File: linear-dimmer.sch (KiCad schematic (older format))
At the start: 32 parts, among them CON1 AVR-ISP-6, IC1 ATTINY85-S, P1 POWER, P2 OUTPUT, Q1 Q_NMOS_GDS, SW1 ENCODER, U1 LM78L05ACZ, U2 MCP6401

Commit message: Set some resistor values and FarnellIDs
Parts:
- R1: value R -> 10k
- R5: value R -> 220
- SW1: FarnellID (none) -> 2065047
- U2: FarnellID (none) -> 1852101
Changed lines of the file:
@@
 P 4950 4550
 F 0 "R1" V 5030 4550 50  0000 C CNN
-F 1 "R" V 4950 4550 50  0000 C CNN
+F 1 "10k" V 4950 4550 50  0000 C CNN
 F 2 "Resistors_SMD:R_0603_HandSoldering" V 4880 4550 30  0001 C CNN
 F 3 "" H 4950 4550 30  0000 C CNN
@@
 P 8600 3850
 F 0 "R5" V 8680 3850 50  0000 C CNN
-F 1 "R" V 8600 3850 50  0000 C CNN
+F 1 "220" V 8600 3850 50  0000 C CNN
 F 2 "Resistors_SMD:R_0603_HandSoldering" V 8530 3850 30  0001 C CNN
 F 3 "" H 8600 3850 30  0000 C CNN
@@
 F 2 "Housings_SOT-23_SOT-143_TSOT-6:SOT-23-5" H 7950 3850 60  0001 C CNN
 F 3 "" H 7950 3850 60  0000 C CNN
+F 4 "1852101" H 7950 3850 60  0001 C CNN "FarnellID"
 	1    7950 3850
 	1    0    0    -1
@@
 F 2 "" H 5850 5500 60  0000 C CNN
 F 3 "" H 5850 5500 60  0000 C CNN
+F 4 "2065047" H 5850 5500 60  0001 C CNN "FarnellID"
 	1    5850 5500
 	1    0    0    -1

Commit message: Redraw schematics with just a pot and an opamp current source
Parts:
- removed C5, C8: 1u, Capacitors_SMD:C_0603_HandSoldering, symbol C
- removed C6, C7: 2.2u, Capacitors_SMD:C_0603_HandSoldering, symbol C
- removed CON1: AVR-ISP-6, Pin_Headers:Pin_Header_Straight_2x03, symbol AVR-ISP-6
- removed IC1: ATTINY85-S, Housings_SOIC:SOIJ-8_5.3x5.3mm_Pitch1.27mm, symbol ATTINY85-S
- removed R10, R2, R8, R9: 10k, Resistors_SMD:R_0603_HandSoldering, symbol R
- removed R11, R13: 47k, Resistors_SMD:R_0603_HandSoldering, symbol R
- removed R12: 2.7k, Resistors_SMD:R_0603_HandSoldering, symbol R
- removed R3, R4: 220, Resistors_SMD:R_0603_HandSoldering, symbol R
- removed SW1: ENCODER, symbol ENCODER
- added R?: 36k, Resistors_SMD:R_0603_HandSoldering, symbol R
- added R?: 10k, Resistors_SMD:R_0603_HandSoldering, symbol R
- added RV1: 10k, symbol POT
- added U3: REF3012, Housings_SOT-23_SOT-143_TSOT-6:SOT-23_Handsoldering, symbol REF3012
- R1: value 10k -> 2k
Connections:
- net labels added: +1.2V
- wire segments 44 -> 19
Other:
- moved on the sheet: C1

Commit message: Add buffer opamp, choose a different opamp, redraw the PCB with dumb linead current source
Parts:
- removed U2: MCP6401, Housings_SOT-23_SOT-143_TSOT-6:SOT-23-5, symbol MCP6401
- added U2: MCP6072, Housings_SOIC:SOIC-8_3.9x4.9mm_Pitch1.27mm, symbol LM358N
- RV1: footprint (none) -> w_pth_resistors:trimmer_alps-rk09k1130ah1; FarnellID 191741 -> 1191725
- gave numbers to parts that had none: 2
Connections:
- wire segments 19 -> 23
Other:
- moved on the sheet: C1, C2, C3, C4, C9, D1, P1, P2, Q1, R1, R14, R2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

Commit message: Ready to send to PCB house
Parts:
- removed P2: OUTPUT, w_pin_strip:pin_socket_2, symbol CONN_01X02
- added C5, C6: 1u, Capacitors_SMD:C_0603_HandSoldering, symbol C
- added CON1: BARREL_JACK, symbol BARREL_JACK
- added D2: RED, w_smd_leds:Led_0603, symbol Led_Small
- added R10, R9: 10k, Resistors_SMD:R_0603_HandSoldering, symbol R
- added R11: 1M, Resistors_SMD:R_0603_HandSoldering, symbol R
- added R12: 220, Resistors_SMD:R_0603_HandSoldering, symbol R
- added R4: 3.74k, Resistors_SMD:R_0603_HandSoldering, symbol R
- added R8: 78.7k, Resistors_SMD:R_0603_HandSoldering, symbol R
- added SW1: Switch_SPDT_x2, Buttons_Switches_SMD:SW_SPDT_PCM12, symbol Switch_SPDT_x2
- added U4: MCP65R41T, w_smd_trans:sot23-6, symbol MCP65R41T-2402
- D1: value Led_Small -> BLUE
- Q1: value Q_NMOS_GDS -> BUK6207-55C; footprint w_smd_trans:sot223 -> w_smd_trans:d-pak; FarnellID 1769679 -> 1863263
- R2: value 36k -> 17.4k
- R6, R7: footprint Resistors_SMD:R_1206_HandSoldering -> Resistors_SMD:R_2512_HandSoldering; FarnellID 1576602 -> 1100070
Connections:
- net +1.2V: now also R10.1
- net +5V: now also C6.1, U4.6 (V+)
- net GND: now also C5.2, C6.2, D2.2 (C), R9.2, U4.2 (V-)
- net OUTPUT: now also C5.1, CON1.1
- net VCC: now also CON1.2, R8.1
- net at U2.6 (-), U2.7: now also SW1.2 (B); no longer R2.1
- net at R3.1, U2.3 (+): now also R2.1, R4.1; no longer R2.2
- new net: R2.2, SW1.3 (C)
- new net: R4.2, SW1.1 (A)
- new net: R11.2, R12.1, U4.1
- new net: D2.1 (A), R12.2
- new net: R8.2, R9.1, U4.3 (+)
- new net: R10.2, R11.1, U4.4 (_)
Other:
- note added: "1.25V"
- note added: "5mV hysteresis"
- note added: "Battery low detector. The lowest we go is 11V."
- note added: "Prie 11V bus1.24V"
- note added: "lightpipe FarnellID: 2293483"
- note added: "prie 1.25V Vref\n0.909V per 0.5Ohm prie 1.8A išėjime\n0.450V per 0.5Ohm prie 0.9A išėjime"
- moved on the sheet: C1, C2, C3, C4, C9, D1, P1, Q1, R1, R14, R2, R3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

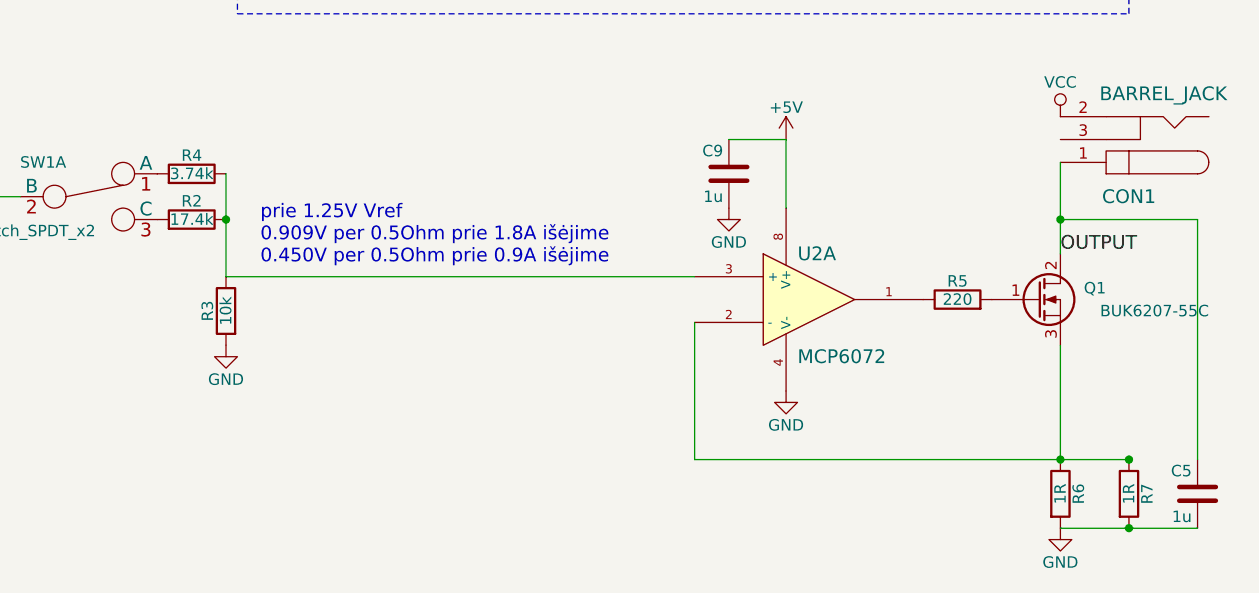
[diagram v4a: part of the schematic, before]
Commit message: Update the value for shunt resistors, recalculate divider values accordingly
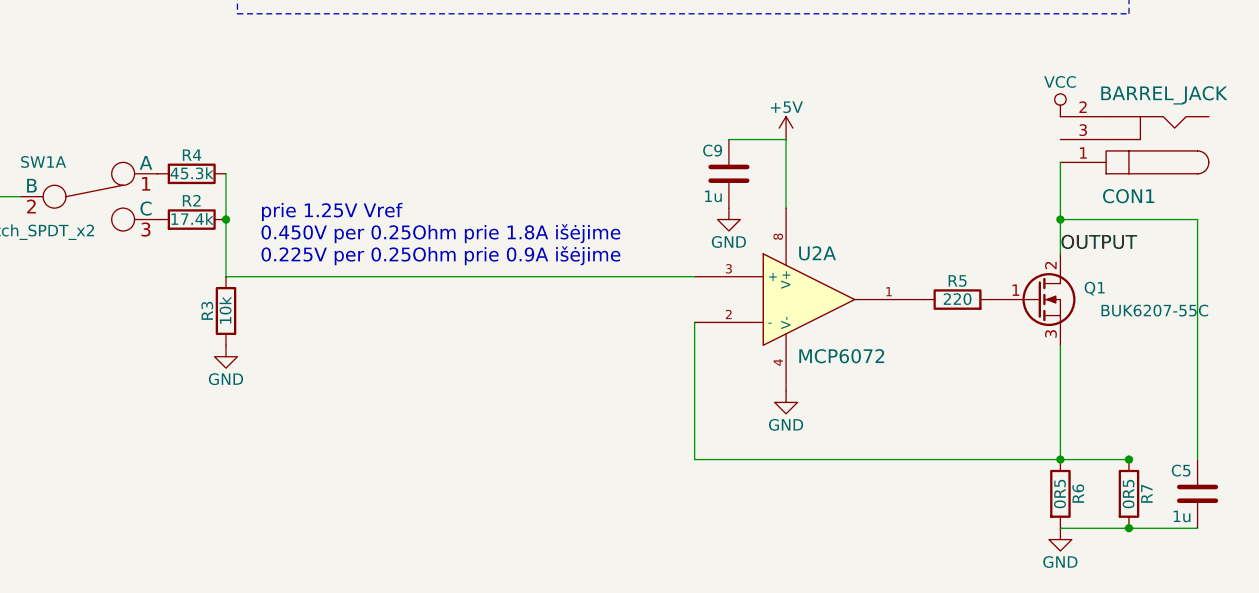
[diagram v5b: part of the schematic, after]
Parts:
- R4: value 3.74k -> 45.3k
- R6, R7: value 1R -> 0R5
- R8: FarnellID (none) -> 1527679
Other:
- note added: "prie 1.25V Vref\n0.450V per 0.25Ohm prie 1.8A išėjime\n0.225V per 0.25Ohm prie 0.9A išėjime"
- note removed: "prie 1.25V Vref\n0.909V per 0.5Ohm prie 1.8A išėjime\n0.450V per 0.5Ohm prie 0.9A išėjime"
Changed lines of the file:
@@
 P 8900 5600
 F 0 "R6" V 8980 5600 50  0000 C CNN
-F 1 "1R" V 8900 5600 50  0000 C CNN
+F 1 "0R5" V 8900 5600 50  0000 C CNN
 F 2 "Resistors_SMD:R_2512_HandSoldering" V 8830 5600 30  0001 C CNN
 F 3 "" H 8900 5600 30  0000 C CNN
@@
 P 9200 5600
 F 0 "R7" V 9280 5600 50  0000 C CNN
-F 1 "1R" V 9200 5600 50  0000 C CNN
+F 1 "0R5" V 9200 5600 50  0000 C CNN
 F 2 "Resistors_SMD:R_2512_HandSoldering" V 9130 5600 30  0001 C CNN
 F 3 "" H 9200 5600 30  0000 C CNN
@@
 P 5100 4200
 F 0 "R4" V 5180 4200 50  0000 C CNN
-F 1 "3.74k" V 5100 4200 50  0000 C CNN
+F 1 "45.3k" V 5100 4200 50  0000 C CNN
 F 2 "Resistors_SMD:R_0603_HandSoldering" V 5030 4200 30  0001 C CNN
 F 3 "" H 5100 4200 30  0000 C CNN
@@
 F 2 "Resistors_SMD:R_0603_HandSoldering" V 5580 2150 30  0001 C CNN
 F 3 "" H 5650 2150 30  0000 C CNN
+F 4 "1527679" V 5650 2150 60  0001 C CNN "FarnellID"
 	1    5650 2150
 	-1   0    0    -1
@@
 $EndComp
 Text Notes 5400 4600 0    60   ~ 0
-prie 1.25V Vref\n0.909V per 0.5Ohm prie 1.8A išėjime\n0.450V per 0.5Ohm prie 0.9A išėjime
+prie 1.25V Vref\n0.450V per 0.25Ohm prie 1.8A išėjime\n0.225V per 0.25Ohm prie 0.9A išėjime
 Text Notes 6450 3350 0    60   ~ 0
 5mV hysteresis

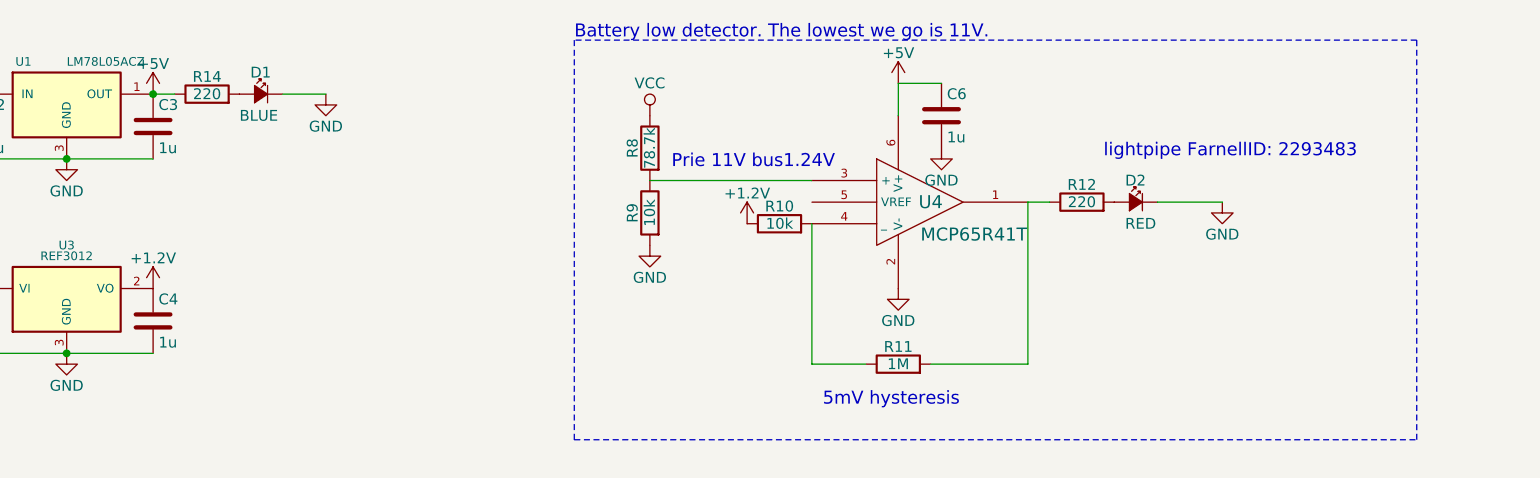
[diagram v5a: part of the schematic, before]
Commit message: Put the power on led to comparator so that blue changes to red on battery low
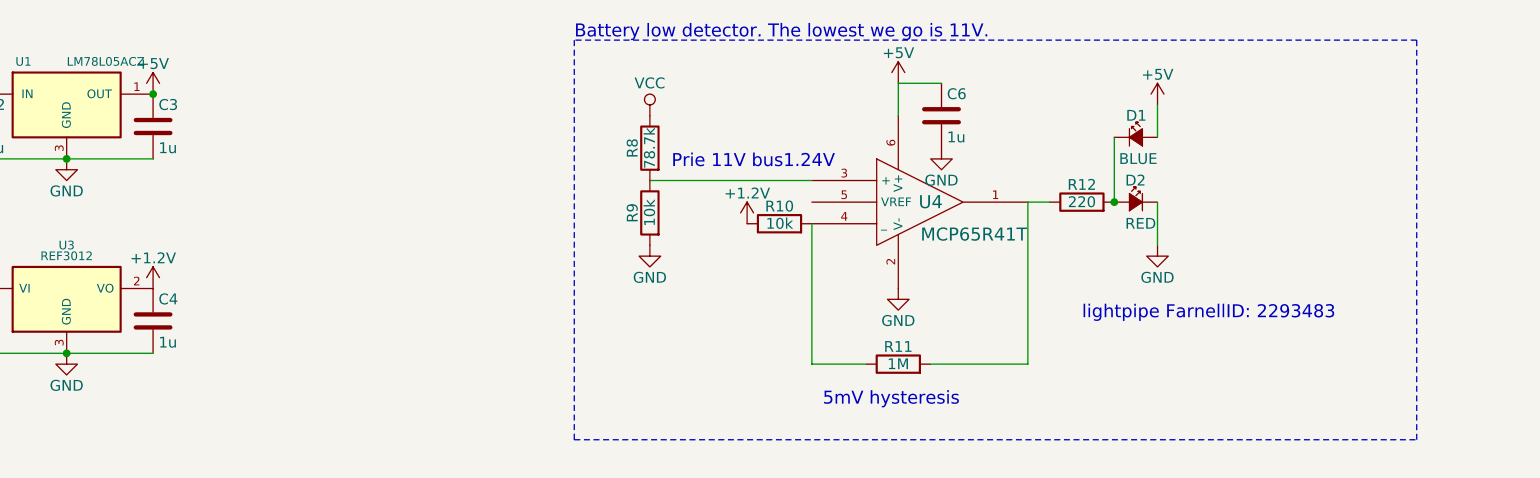
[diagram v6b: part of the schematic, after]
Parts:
- removed R14: 220, Resistors_SMD:R_0603_HandSoldering, symbol R
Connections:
- net +5V: now also D1.1 (A)
- net GND: no longer D1.2 (C)
- net at D2.1 (A), R12.2: now also D1.2 (C)
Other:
- moved on the sheet: D1
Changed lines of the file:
@@
-$EndComp
-$Comp
-L R R14
-U 1 1 559D7E01
-P 3600 1900
-F 0 "R14" V 3680 1900 50  0000 C CNN
-F 1 "220" V 3600 1900 50  0000 C CNN
-F 2 "Resistors_SMD:R_0603_HandSoldering" V 3530 1900 30  0001 C CNN
-F 3 "" H 3600 1900 30  0000 C CNN
-	1    3600 1900
-	0    -1   -1   0
 $EndComp
 $Comp
 L Led_Small D1
 U 1 1 559D7EF2
-P 3850 1900
-F 0 "D1" H 3800 2000 50  0000 L CNN
-F 1 "BLUE" H 3750 1800 50  0000 L CNN
-F 2 "w_smd_leds:Led_0603" V 3850 1900 60  0001 C CNN
-F 3 "" V 3850 1900 60  0000 C CNN
-	1    3850 1900
-	1    0    0    -1
-$EndComp
-$Comp
-L GND #PWR011
-U 1 1 559D7F73
-P 4150 1900
-F 0 "#PWR011" H 4150 1650 50  0001 C CNN
-F 1 "GND" H 4150 1750 50  0000 C CNN
-F 2 "" H 4150 1900 60  0000 C CNN
-F 3 "" H 4150 1900 60  0000 C CNN
-	1    4150 1900
-	1    0    0    -1
+P 7900 2100
+F 0 "D1" H 7850 2200 50  0000 L CNN
+F 1 "BLUE" H 7800 2000 50  0000 L CNN
+F 2 "w_smd_leds:Led_0603" V 7900 2100 60  0001 C CNN
+F 3 "" V 7900 2100 60  0000 C CNN
+	1    7900 2100
+	-1   0    0    -1
 $EndComp
 $Comp
@@
 Wire Wire Line
 	7700 4050 7700 4350
-Wire Wire Line
-	3450 1900 3350 1900
 Connection ~ 3350 1900
-Wire Wire Line
-	3950 1900 4150 1900
 Wire Wire Line
 	2650 4200 3200 4200
@@
 L GND #PWR018
 U 1 1 5601D857
-P 8300 2400
-F 0 "#PWR018" H 8300 2150 50  0001 C CNN
-F 1 "GND" H 8300 2250 50  0000 C CNN
-F 2 "" H 8300 2400 60  0000 C CNN
-F 3 "" H 8300 2400 60  0000 C CNN
-	1    8300 2400
-	1    0    0    -1
-$EndComp
-Text Notes 7750 2200 0    60   ~ 0
+P 8000 2600
+F 0 "#PWR018" H 8000 2350 50  0001 C CNN
+F 1 "GND" H 8000 2450 50  0000 C CNN
+F 2 "" H 8000 2600 60  0000 C CNN
+F 3 "" H 8000 2600 60  0000 C CNN
+	1    8000 2600
+	1    0    0    -1
+$EndComp
+Text Notes 7650 2950 0    60   ~ 0
 lightpipe FarnellID: 2293483
 $Comp
@@
 Text Notes 5300 1650 0    60   ~ 0
 Battery low detector. The lowest we go is 11V.
-Wire Wire Line
-	8000 2400 8300 2400
 $Comp
 L MCP65R41T-2402 U4
@@
 	9500 4400 8900 4400
 Connection ~ 8900 4400
+Connection ~ 7800 2400
+$Comp
+L +5V #PWR?
+U 1 1 56292244
+P 8000 1950
+F 0 "#PWR?" H 8000 1800 50  0001 C CNN
+F 1 "+5V" H 8000 2090 50  0000 C CNN
+F 2 "" H 8000 1950 60  0000 C CNN
+F 3 "" H 8000 1950 60  0000 C CNN
+	1    8000 1950
+	1    0    0    -1
+$EndComp
+Wire Wire Line
+	7800 2400 7800 2100
+Wire Wire Line
+	8000 1950 8000 2100
+Wire Wire Line
+	8000 2400 8000 2600
 $EndSCHEMATC

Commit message: Schematic changes after new kicad version
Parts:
- D1, D2: symbol Led_Small -> Led_Small-RESCUE-linear-dimmer
- Q1: symbol Q_NMOS_GDS -> Q_NMOS_GDS-RESCUE-linear-dimmer
- U1: symbol LM78L05ACZ -> LM78L05ACZ-RESCUE-linear-dimmer
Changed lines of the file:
@@
 EESchema Schematic File Version 2
+LIBS:linear-dimmer-rescue
 LIBS:power
 LIBS:device
@@
 $EndComp
 $Comp
-L LM78L05ACZ U1
+L LM78L05ACZ-RESCUE-linear-dimmer U1
 U 1 1 559063B7
 P 2950 1950
@@
 $EndComp
 $Comp
-L Q_NMOS_GDS Q1
+L Q_NMOS_GDS-RESCUE-linear-dimmer Q1
 U 1 1 55906DA2
 P 8800 4750
@@
 $EndComp
 $Comp
-L Led_Small D1
+L Led_Small-RESCUE-linear-dimmer D1
 U 1 1 559D7EF2
 P 7900 2100
@@
 $EndComp
 $Comp
-L GND #PWR012
+L GND #PWR011
 U 1 1 55E4A652
 P 2700 4550
-F 0 "#PWR012" H 2700 4300 50  0001 C CNN
+F 0 "#PWR011" H 2700 4300 50  0001 C CNN
 F 1 "GND" H 2700 4400 50  0000 C CNN
 F 2 "" H 2700 4550 60  0000 C CNN
@@
 $EndComp
 $Comp
-L +1.2V #PWR013
+L +1.2V #PWR012
 U 1 1 55E4CC47
 P 3350 2800
-F 0 "#PWR013" H 3350 2650 50  0001 C CNN
+F 0 "#PWR012" H 3350 2650 50  0001 C CNN
 F 1 "+1.2V" H 3350 2940 50  0000 C CNN
 F 2 "" H 3350 2800 60  0000 C CNN
@@
 $EndComp
 $Comp
-L +1.2V #PWR014
+L +1.2V #PWR013
 U 1 1 55E4CC8F
 P 2500 3950
-F 0 "#PWR014" H 2500 3800 50  0001 C CNN
+F 0 "#PWR013" H 2500 3800 50  0001 C CNN
 F 1 "+1.2V" H 2500 4090 50  0000 C CNN
 F 2 "" H 2500 3950 60  0000 C CNN
@@
 $EndComp
 $Comp
-L GND #PWR015
+L GND #PWR014
 U 1 1 55E4D092
 P 5250 4950
-F 0 "#PWR015" H 5250 4700 50  0001 C CNN
+F 0 "#PWR014" H 5250 4700 50  0001 C CNN
 F 1 "GND" H 5250 4800 50  0000 C CNN
 F 2 "" H 5250 4950 60  0000 C CNN
@@
 $EndComp
 $Comp
-L GND #PWR016
+L GND #PWR015
 U 1 1 55FF0591
 P 3600 4700
-F 0 "#PWR016" H 3600 4450 50  0001 C CNN
+F 0 "#PWR015" H 3600 4450 50  0001 C CNN
 F 1 "GND" H 3600 4550 50  0000 C CNN
 F 2 "" H 3600 4700 60  0000 C CNN
@@
 $EndComp
 $Comp
-L +5V #PWR017
+L +5V #PWR016
 U 1 1 55FF0610
 P 3600 3900
-F 0 "#PWR017" H 3600 3750 50  0001 C CNN
+F 0 "#PWR016" H 3600 3750 50  0001 C CNN
 F 1 "+5V" H 3600 4040 50  0000 C CNN
 F 2 "" H 3600 3900 60  0000 C CNN
@@
 $EndComp
 $Comp
-L Led_Small D2
+L Led_Small-RESCUE-linear-dimmer D2
 U 1 1 5601D7BE
 P 7900 2400
@@
 $EndComp
 $Comp
-L GND #PWR018
+L GND #PWR017
 U 1 1 5601D857
 P 8000 2600
-F 0 "#PWR018" H 8000 2350 50  0001 C CNN
+F 0 "#PWR017" H 8000 2350 50  0001 C CNN
 F 1 "GND" H 8000 2450 50  0000 C CNN
 F 2 "" H 8000 2600 60  0000 C CNN
@@
 lightpipe FarnellID: 2293483
 $Comp
-L +5V #PWR019
+L +5V #PWR018
 U 1 1 5601D9EF
 P 6800 1850
-F 0 "#PWR019" H 6800 1700 50  0001 C CNN
+F 0 "#PWR018" H 6800 1700 50  0001 C CNN
 F 1 "+5V" H 6800 1990 50  0000 C CNN
 F 2 "" H 6800 1850 60  0000 C CNN
@@
 $EndComp
 $Comp
-L GND #PWR020
+L GND #PWR019
 U 1 1 5601DA4B
 P 6800 2800
-F 0 "#PWR020" H 6800 2550 50  0001 C CNN
+F 0 "#PWR019" H 6800 2550 50  0001 C CNN
 F 1 "GND" H 6800 2650 50  0000 C CNN
 F 2 "" H 6800 2800 60  0000 C CNN
@@
 $EndComp
 $Comp
-L VCC #PWR021
+L VCC #PWR020
 U 1 1 5601DAF8
 P 5650 2000
-F 0 "#PWR021" H 5650 1850 50  0001 C CNN
+F 0 "#PWR020" H 5650 1850 50  0001 C CNN
 F 1 "VCC" H 5650 2150 50  0000 C CNN
 F 2 "" H 5650 2000 60  0000 C CNN
@@
 $EndComp
 $Comp
-L GND #PWR022
+L GND #PWR021
 U 1 1 5601DC67
 P 5650 2600
-F 0 "#PWR022" H 5650 2350 50  0001 C CNN
+F 0 "#PWR021" H 5650 2350 50  0001 C CNN
 F 1 "GND" H 5650 2450 50  0000 C CNN
 F 2 "" H 5650 2600 60  0000 C CNN
@@
 $EndComp
 $Comp
-L +1.2V #PWR023
+L +1.2V #PWR022
 U 1 1 56038379
 P 6100 2500
-F 0 "#PWR023" H 6100 2350 50  0001 C CNN
+F 0 "#PWR022" H 6100 2350 50  0001 C CNN
 F 1 "+1.2V" H 6100 2640 50  0000 C CNN
 F 2 "" H 6100 2500 60  0000 C CNN
@@
 $EndComp
 $Comp
-L GND #PWR024
+L GND #PWR023
 U 1 1 56054695
 P 7000 2150
-F 0 "#PWR024" H 7000 1900 50  0001 C CNN
+F 0 "#PWR023" H 7000 1900 50  0001 C CNN
 F 1 "GND" H 7000 2000 50  0000 C CNN
 F 2 "" H 7000 2150 60  0000 C CNN
@@
 Connection ~ 7800 2400
 $Comp
-L +5V #PWR?
+L +5V #PWR024
 U 1 1 56292244
 P 8000 1950
-F 0 "#PWR?" H 8000 1800 50  0001 C CNN
+F 0 "#PWR024" H 8000 1800 50  0001 C CNN
 F 1 "+5V" H 8000 2090 50  0000 C CNN
 F 2 "" H 8000 1950 60  0000 C CNN
